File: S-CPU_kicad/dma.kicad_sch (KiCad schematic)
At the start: 112 parts

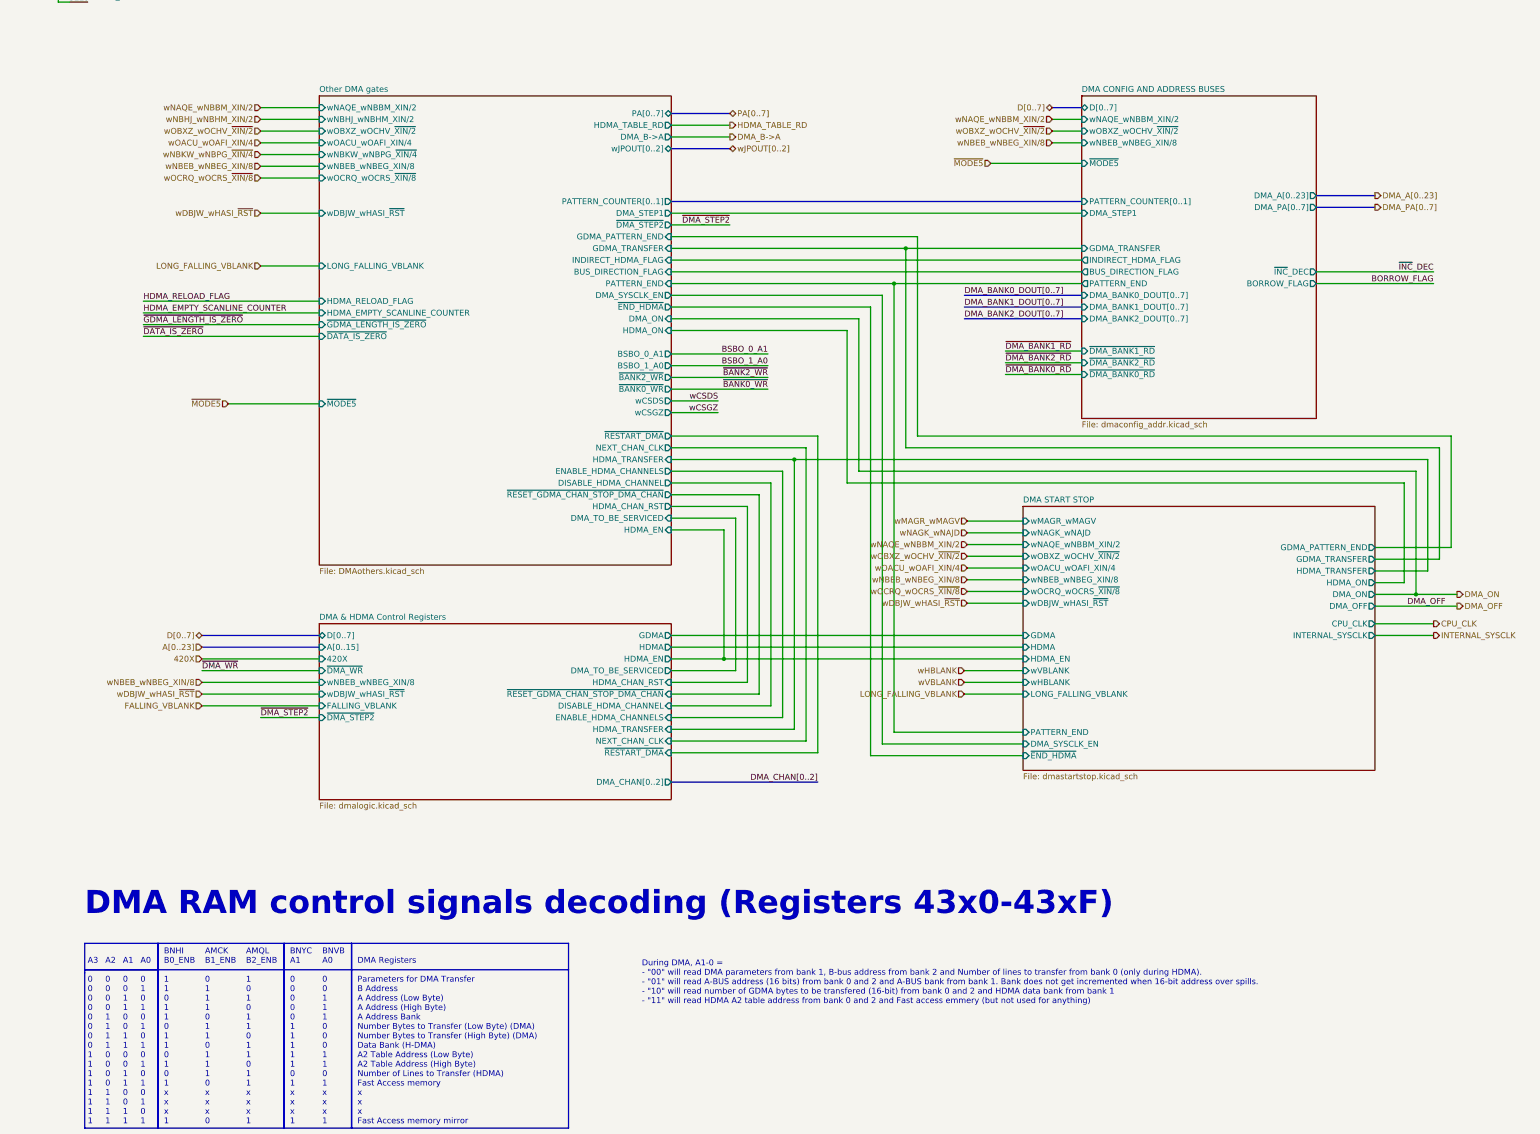
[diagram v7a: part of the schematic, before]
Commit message: More notes added to detail HDMA steps
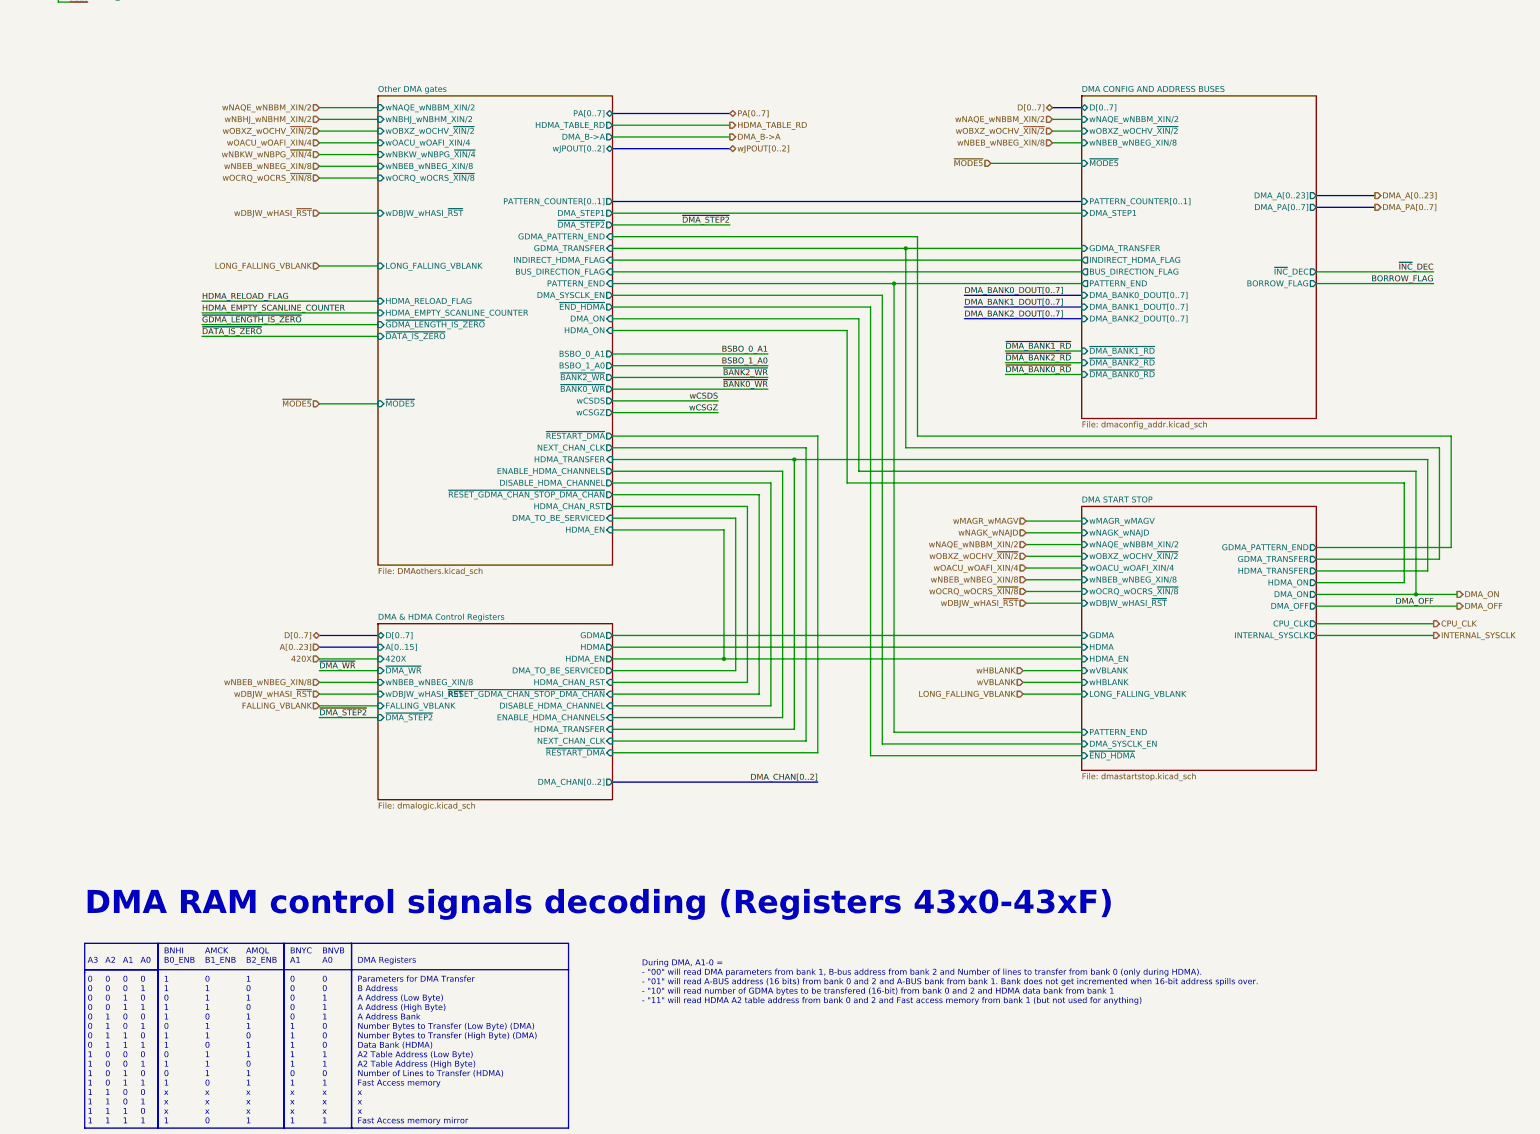
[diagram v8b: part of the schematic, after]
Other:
- note added: "DMA Registers Parameters for DMA Transfer B Address A Address (Low Byte) A Address (High Byte) A Address Bank Number Bytes to Transfer (Low Byte) (DMA) Number Bytes to Transfer (High Byte) (DMA) Data Bank (HDMA) A2 Table Address (Low Byte) A2 Table Address (High Byte) Number of Lines to Transfer (HDMA) Fast Access memory x x x Fast Access memory mirror"
- note added: "During DMA, A1-0 = - "00" will read DMA parameters from bank 1, B-bus address from bank 2 and Number of lines to transfer from bank 0 (only during HDMA). - "01" will read A-BUS address (16 bits) from bank 0 and 2 and A-BUS bank from bank 1. Bank does not get incremented when 16-bit address spills over. - "10" will read number of GDMA bytes to be transfered (16-bit) from bank 0 and 2 and HDMA data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"
- note removed: "DMA Registers Parameters for DMA Transfer B Address A Address (Low Byte) A Address (High Byte) A Address Bank Number Bytes to Transfer (Low Byte) (DMA) Number Bytes to Transfer (High Byte) (DMA) Data Bank (H-DMA) A2 Table Address (Low Byte) A2 Table Address (High Byte) Number of Lines to Transfer (HDMA) Fast Access memory x x x Fast Access memory mirror"
- note removed: "During DMA, A1-0 = - "00" will read DMA parameters from bank 1, B-bus address from bank 2 and Number of lines to transfer from bank 0 (only during HDMA). - "01" will read A-BUS address (16 bits) from bank 0 and 2 and A-BUS bank from bank 1. Bank does not get incremented when 16-bit address over spills. - "10" will read number of GDMA bytes to be transfered (16-bit) from bank 0 and 2 and HDMA data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"
